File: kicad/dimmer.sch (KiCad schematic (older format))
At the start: 12 parts, among them IC1 ATTINY85-P, P1 CONN_01X02, P2 CONN_01X02, Q1 Q_NMOS_GDS, SW1 TACTILE_SW, SW2 TACTILE_SW, SW3 TACTILE_SW, SW4 TACTILE_SW, U1 MC78L05ACH

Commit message: pcb progress
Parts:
- removed SW1, SW3: TACTILE_SW, Buttons_Switches_ThroughHole:SW_TH_Tactile_Omron_B3F-10xx, symbol TACTILE_SW
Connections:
- net +12V: now also P1.1 (P1); no longer P1.2 (P2)
- net GND: now also P1.2 (P2), SW4.4; no longer P1.1 (P1), SW4.3
- net at IC1.2 (PB3(XTAL1/CLKI/OC1B/ADC3/PCINT3)): now also SW4.2; no longer SW4.1
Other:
- moved on the sheet: SW2
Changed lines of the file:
@@
 LIBS:irlz44nto220v
 LIBS:button
+LIBS:dimmer-cache
 EELAYER 25 0
 EELAYER END
@@
 $EndComp
 $Comp
-L +5V #PWR02
+L +5V #PWR01
 U 1 1 57A7313A
 P 3900 2000
-F 0 "#PWR02" H 3900 1850 50  0001 C CNN
+F 0 "#PWR01" H 3900 1850 50  0001 C CNN
 F 1 "+5V" H 3900 2140 50  0000 C CNN
 F 2 "" H 3900 2000 50  0000 C CNN
@@
 $EndComp
 $Comp
-L +12V #PWR03
+L +12V #PWR02
 U 1 1 57A73161
 P 2550 2000
-F 0 "#PWR03" H 2550 1850 50  0001 C CNN
+F 0 "#PWR02" H 2550 1850 50  0001 C CNN
 F 1 "+12V" H 2550 2140 50  0000 C CNN
 F 2 "" H 2550 2000 50  0000 C CNN
@@
 F 3 "" H 2150 3100 50  0000 C CNN
 	1    2150 3100
-	-1   0    0    1
-$EndComp
-$Comp
-L +5V #PWR06
+	-1   0    0    -1
+$EndComp
+$Comp
+L +5V #PWR03
 U 1 1 57A73318
 P 3550 2000
-F 0 "#PWR06" H 3550 1850 50  0001 C CNN
+F 0 "#PWR03" H 3550 1850 50  0001 C CNN
 F 1 "+5V" H 3550 2140 50  0000 C CNN
 F 2 "" H 3550 2000 50  0000 C CNN
@@
 $EndComp
 $Comp
-L +5V #PWR09
+L +5V #PWR04
 U 1 1 57A7351F
 P 6700 2000
-F 0 "#PWR09" H 6700 1850 50  0001 C CNN
+F 0 "#PWR04" H 6700 1850 50  0001 C CNN
 F 1 "+5V" H 6700 2140 50  0000 C CNN
 F 2 "" H 6700 2000 50  0000 C CNN
@@
 $EndComp
 $Comp
-L TACTILE_SW SW3
-U 1 1 57A73C91
+L TACTILE_SW SW2
+U 1 1 57A73CC7
 P 7300 2750
-F 0 "SW3" H 7450 2860 50  0000 C CNN
+F 0 "SW2" H 7450 2860 50  0000 C CNN
 F 1 "TACTILE_SW" H 7320 2610 50  0001 C CNN
 F 2 "Buttons_Switches_ThroughHole:SW_TH_Tactile_Omron_B3F-10xx" H 7300 2750 50  0001 C CNN
@@
 	1    0    0    -1
 $EndComp
-$Comp
-L TACTILE_SW SW2
-U 1 1 57A73CC7
-P 7300 2450
-F 0 "SW2" H 7450 2560 50  0000 C CNN
-F 1 "TACTILE_SW" H 7320 2310 50  0001 C CNN
-F 2 "Buttons_Switches_ThroughHole:SW_TH_Tactile_Omron_B3F-10xx" H 7300 2450 50  0001 C CNN
-F 3 "" H 7300 2450 50  0000 C CNN
-	1    7300 2450
-	1    0    0    -1
-$EndComp
-$Comp
-L TACTILE_SW SW1
-U 1 1 57A73D21
-P 7300 2150
-F 0 "SW1" H 7450 2260 50  0000 C CNN
-F 1 "TACTILE_SW" H 7320 2010 50  0001 C CNN
-F 2 "Buttons_Switches_ThroughHole:SW_TH_Tactile_Omron_B3F-10xx" H 7300 2150 50  0001 C CNN
-F 3 "" H 7300 2150 50  0000 C CNN
-	1    7300 2150
-	1    0    0    -1
-$EndComp
 Wire Wire Line
 	3900 3350 3900 3450
@@
 	8050 3350 8050 3450
 Wire Wire Line
-	6600 3150 7050 3150
-Wire Wire Line
-	7050 3150 7050 3050
-Wire Wire Line
-	7050 3050 7100 3050
-Wire Wire Line
-	6600 3050 7000 3050
-Wire Wire Line
-	7000 3050 7000 2750
-Wire Wire Line
-	7000 2750 7100 2750
+	6600 3150 7100 3150
 Wire Wire Line
 	6600 2950 6950 2950
 Wire Wire Line
-	6950 2950 6950 2450
-Wire Wire Line
-	6950 2450 7100 2450
-Wire Wire Line
-	6600 2850 6900 2850
-Wire Wire Line
-	6900 2850 6900 2150
-Wire Wire Line
-	6900 2150 7100 2150
-Wire Wire Line
-	7500 2150 7600 2150
-Wire Wire Line
-	7600 2150 7600 3450
-Wire Wire Line
-	7500 2450 7600 2450
-Connection ~ 7600 2450
+	6950 2950 6950 2750
+Wire Wire Line
+	6950 2750 7100 2750
 Wire Wire Line
 	7500 2750 7600 2750
-Connection ~ 7600 2750
-Wire Wire Line
-	7500 3050 7600 3050
-Connection ~ 7600 3050
 Wire Wire Line
 	8050 2950 8050 2750
 $Comp
-L +12V #PWR012
+L +12V #PWR05
 U 1 1 57A7493A
 P 8050 2000
-F 0 "#PWR012" H 8050 1850 50  0001 C CNN
+F 0 "#PWR05" H 8050 1850 50  0001 C CNN
 F 1 "+12V" H 8050 2140 50  0000 C CNN
 F 2 "" H 8050 2000 50  0000 C CNN
@@
 out
 $Comp
-L GND #PWR?
+L GND #PWR06
 U 1 1 57A75236
 P 2400 3450
-F 0 "#PWR?" H 2400 3200 50  0001 C CNN
+F 0 "#PWR06" H 2400 3200 50  0001 C CNN
 F 1 "GND" H 2400 3300 50  0000 C CNN
 F 2 "" H 2400 3450 50  0000 C CNN
@@
 $EndComp
 $Comp
-L GND #PWR?
+L GND #PWR07
 U 1 1 57A7526C
 P 2550 3450
-F 0 "#PWR?" H 2550 3200 50  0001 C CNN
+F 0 "#PWR07" H 2550 3200 50  0001 C CNN
 F 1 "GND" H 2550 3300 50  0000 C CNN
 F 2 "" H 2550 3450 50  0000 C CNN
@@
 $EndComp
 $Comp
-L GND #PWR?
+L GND #PWR08
 U 1 1 57A7529B
 P 3050 3450
-F 0 "#PWR?" H 3050 3200 50  0001 C CNN
+F 0 "#PWR08" H 3050 3200 50  0001 C CNN
 F 1 "GND" H 3050 3300 50  0000 C CNN
 F 2 "" H 3050 3450 50  0000 C CNN
@@
 $EndComp
 $Comp
-L GND #PWR?
+L GND #PWR09
 U 1 1 57A752E2
 P 3550 3450
-F 0 "#PWR?" H 3550 3200 50  0001 C CNN
+F 0 "#PWR09" H 3550 3200 50  0001 C CNN
 F 1 "GND" H 3550 3300 50  0000 C CNN
 F 2 "" H 3550 3450 50  0000 C CNN
@@
 $EndComp
 $Comp
-L GND #PWR?
+L GND #PWR010
 U 1 1 57A75311
 P 3900 3450
-F 0 "#PWR?" H 3900 3200 50  0001 C CNN
+F 0 "#PWR010" H 3900 3200 50  0001 C CNN
 F 1 "GND" H 3900 3300 50  0000 C CNN
 F 2 "" H 3900 3450 50  0000 C CNN
@@
 $EndComp
 $Comp
-L GND #PWR?
+L GND #PWR011
 U 1 1 57A753DC
 P 7600 3450
-F 0 "#PWR?" H 7600 3200 50  0001 C CNN
+F 0 "#PWR011" H 7600 3200 50  0001 C CNN
 F 1 "GND" H 7600 3300 50  0000 C CNN
 F 2 "" H 7600 3450 50  0000 C CNN
@@
 $EndComp
 $Comp
-L GND #PWR?
+L GND #PWR012
 U 1 1 57A7540B
 P 8050 3450
-F 0 "#PWR?" H 8050 3200 50  0001 C CNN
+F 0 "#PWR012" H 8050 3200 50  0001 C CNN
 F 1 "GND" H 8050 3300 50  0000 C CNN
 F 2 "" H 8050 3450 50  0000 C CNN
@@
 	1    0    0    -1
 $EndComp
+Wire Wire Line
+	7600 2750 7600 3450
+Wire Wire Line
+	7500 3150 7600 3150
+Connection ~ 7600 3150
 $EndSCHEMATC

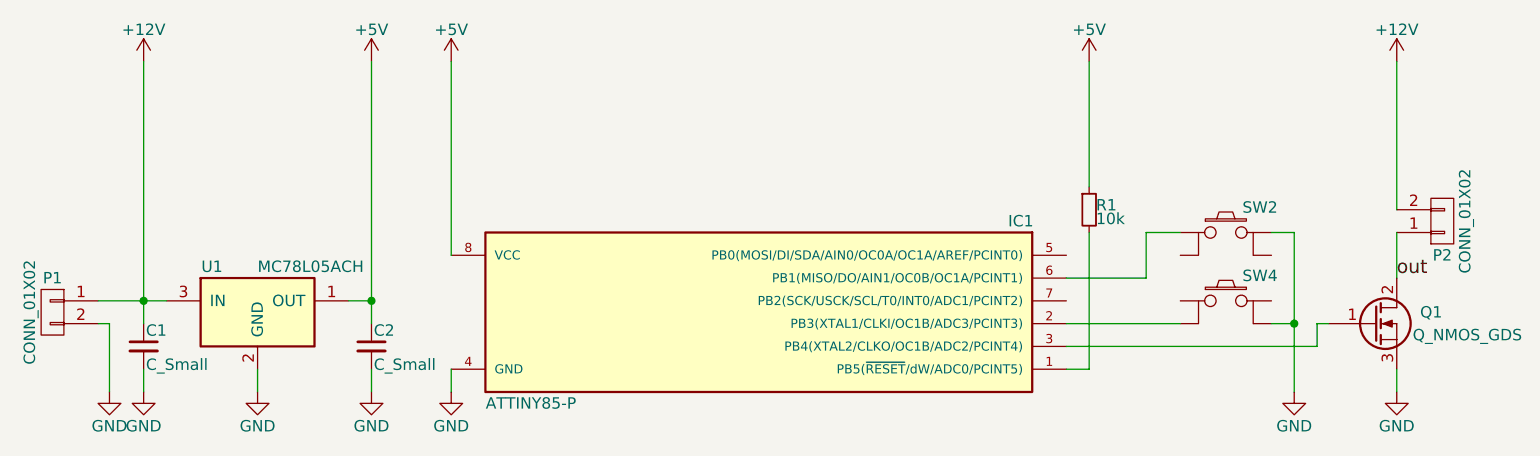
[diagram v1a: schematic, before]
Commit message: pcb: changing sides
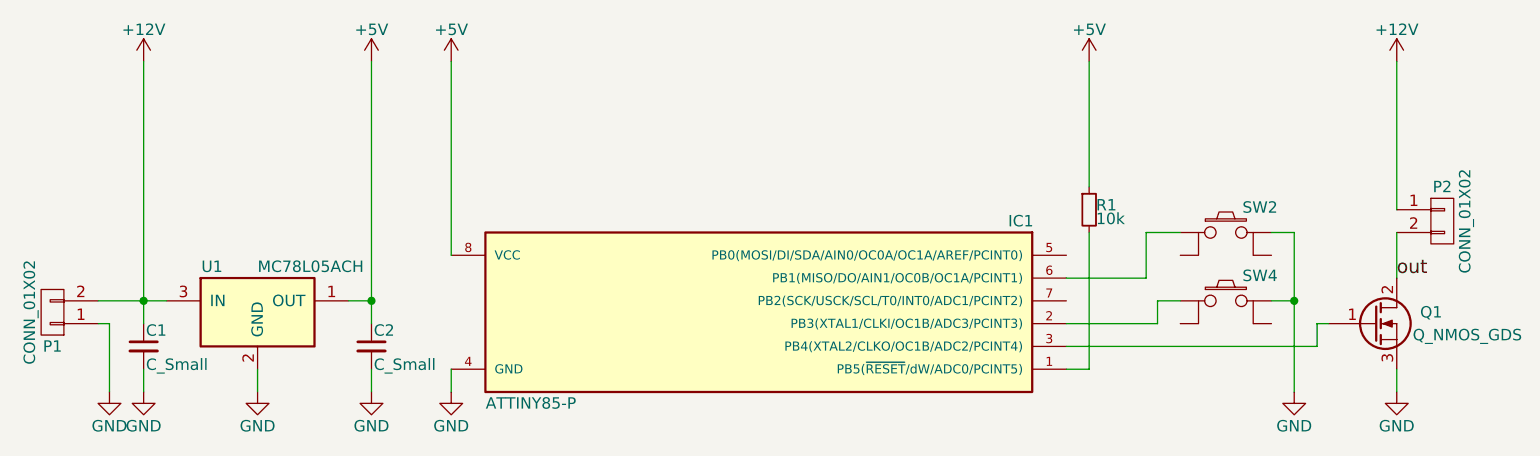
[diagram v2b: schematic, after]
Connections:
- net +12V: now also P1.2 (P2), P2.1 (P1); no longer P1.1 (P1), P2.2 (P2)
- net GND: now also P1.1 (P1), SW4.3; no longer P1.2 (P2), SW4.4
- net out: now also P2.2 (P2); no longer P2.1 (P1)
- net at IC1.2 (PB3(XTAL1/CLKI/OC1B/ADC3/PCINT3)): now also SW4.1; no longer SW4.2
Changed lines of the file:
@@
 F 3 "" H 2150 3100 50  0000 C CNN
 	1    2150 3100
-	-1   0    0    -1
+	-1   0    0    1
 $EndComp
 $Comp
@@
 F 3 "" H 8250 2700 50  0000 C CNN
 	1    8250 2700
-	1    0    0    1
+	1    0    0    -1
 $EndComp
 $Comp
@@
 	8050 3350 8050 3450
 Wire Wire Line
-	6600 3150 7100 3150
-Wire Wire Line
 	6600 2950 6950 2950
 Wire Wire Line
@@
 	7600 2750 7600 3450
 Wire Wire Line
-	7500 3150 7600 3150
-Connection ~ 7600 3150
+	6600 3150 7000 3150
+Wire Wire Line
+	7000 3150 7000 3050
+Wire Wire Line
+	7000 3050 7100 3050
+Wire Wire Line
+	7500 3050 7600 3050
+Connection ~ 7600 3050
 $EndSCHEMATC

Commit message: pcb: proper t85 footprint
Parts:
- removed IC1: ATTINY85-P, Housings_SSOP:TSSOP-8_3x3mm_Pitch0.65mm, symbol ATTINY85-P
- removed R1: 10k, Resistors_SMD:R_0805, symbol R_Small
- added IC1: ATTINY85-S, SMD_Packages:SOIC-8-N, symbol ATTINY85-S
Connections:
- net +5V: now also IC1.8 (VCC)
- net GND: now also IC1.4 (GND)
- net at SW4.1: now also IC1.2 (PB3(XTAL1/CLKI/OC1B/ADC3/PCINT3))
- net at Q1.1 (G): now also IC1.3 (PB4(XTAL2/CLKO/OC1B/ADC2/PCINT4))
- net at SW2.1: now also IC1.6 (PB1(MISO/DO/AIN1/OC0B/OC1A/PCINT1))
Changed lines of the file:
@@
 $EndDescr
-$Comp
-L ATTINY85-P IC1
-U 1 1 57A730B7
-P 5250 3100
-F 0 "IC1" H 4100 3500 50  0000 C CNN
-F 1 "ATTINY85-P" H 6250 2700 50  0000 C CNN
-F 2 "Housings_SSOP:TSSOP-8_3x3mm_Pitch0.65mm" H 6250 3100 50  0001 C CIN
-F 3 "" H 5250 3100 50  0000 C CNN
-	1    5250 3100
-	-1   0    0    -1
-$EndComp
 $Comp
 L +5V #PWR01
@@
 $EndComp
 $Comp
-L R_Small R1
-U 1 1 57A734B2
-P 6700 2650
-F 0 "R1" H 6730 2670 50  0000 L CNN
-F 1 "10k" H 6730 2610 50  0000 L CNN
-F 2 "Resistors_SMD:R_0805" H 6700 2650 50  0001 C CNN
-F 3 "" H 6700 2650 50  0000 C CNN
-	1    6700 2650
-	1    0    0    -1
-$EndComp
-$Comp
-L +5V #PWR04
-U 1 1 57A7351F
-P 6700 2000
-F 0 "#PWR04" H 6700 1850 50  0001 C CNN
-F 1 "+5V" H 6700 2140 50  0000 C CNN
-F 2 "" H 6700 2000 50  0000 C CNN
-F 3 "" H 6700 2000 50  0000 C CNN
-	1    6700 2000
-	1    0    0    -1
-$EndComp
-$Comp
 L Q_NMOS_GDS Q1
 U 1 1 57A7361A
@@
 	2550 3450 2550 3350
 Wire Wire Line
-	6600 3350 6700 3350
-Wire Wire Line
-	6700 3350 6700 2750
-Wire Wire Line
-	6700 2550 6700 2000
-Wire Wire Line
 	6600 3250 7700 3250
 Wire Wire Line
@@
 	7500 3050 7600 3050
 Connection ~ 7600 3050
+$Comp
+L ATTINY85-S IC1
+U 1 1 57AF71E0
+P 5250 3100
+F 0 "IC1" H 5250 3707 50  0000 C CNN
+F 1 "ATTINY85-S" H 5250 3616 50  0000 C CNN
+F 2 "SMD_Packages:SOIC-8-N" H 5250 3525 50  0000 C CIN
+F 3 "" H 5250 3100 50  0000 C CNN
+	1    5250 3100
+	-1   0    0    -1
+$EndComp
 $EndSCHEMATC
